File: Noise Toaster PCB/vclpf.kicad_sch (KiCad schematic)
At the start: 27 parts, among them Q5 2N5457, U2 LM324, X12 Conn_01x01_Pin

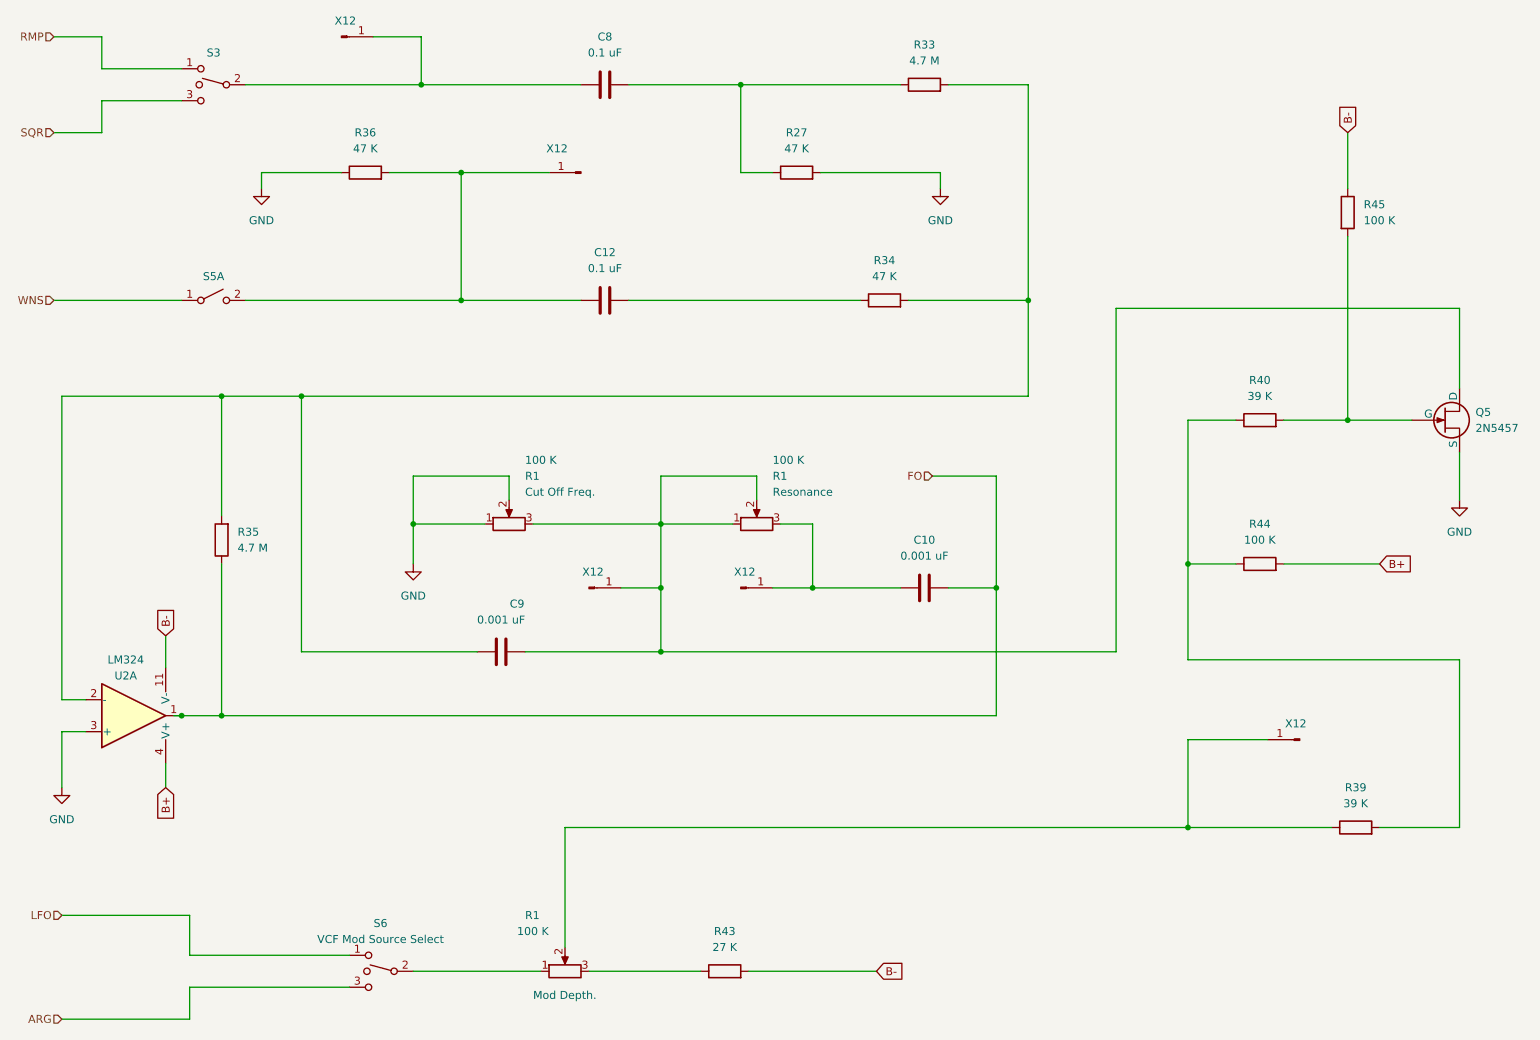
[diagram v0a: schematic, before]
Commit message: updated schematics
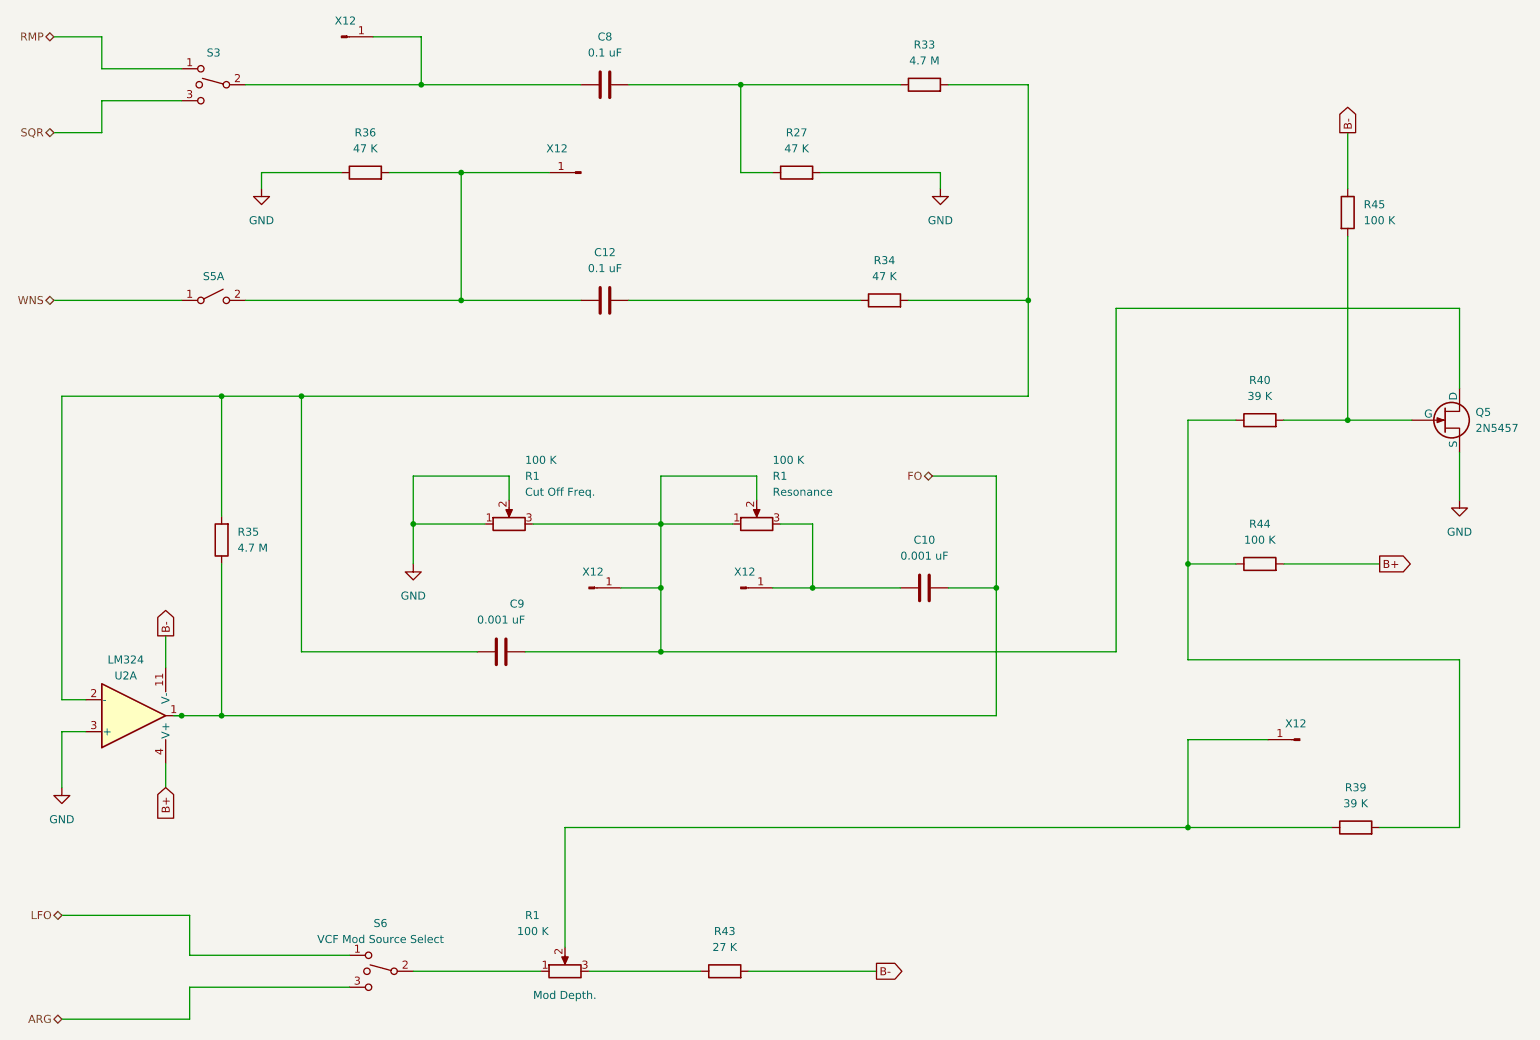
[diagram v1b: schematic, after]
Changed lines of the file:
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@@
     (stroke (width 0) (type default))
   )
-  (global_label "B-" (shape input) (at 48.26 125.73 90) (fields_autoplaced)
+  (global_label "B-" (shape output) (at 48.26 125.73 90) (fields_autoplaced)
     (effects (font (size 1.27 1.27)) (justify left))
     (property "Intersheetrefs" "${INTERSHEET_REFS}" (at 48.26 119.9024 90)
@@
     )
   )
-  (global_label "B-" (shape input) (at 236.22 45.72 90) (fields_autoplaced)
+  (global_label "B-" (shape output) (at 236.22 45.72 90) (fields_autoplaced)
     (effects (font (size 1.27 1.27)) (justify left))
     (property "Intersheetrefs" "${INTERSHEET_REFS}" (at 236.22 39.8924 90)
@@
     )
   )
-  (global_label "B+" (shape input) (at 241.3 114.3 0) (fields_autoplaced)
+  (global_label "B+" (shape output) (at 241.3 114.3 0) (fields_autoplaced)
     (effects (font (size 1.27 1.27)) (justify left))
     (property "Intersheetrefs" "${INTERSHEET_REFS}" (at 247.1276 114.3 0)
@@
     )
   )
-  (global_label "B-" (shape input) (at 161.29 179.07 0) (fields_autoplaced)
+  (global_label "B-" (shape output) (at 161.29 179.07 0) (fields_autoplaced)
     (effects (font (size 1.27 1.27)) (justify left))
     (property "Intersheetrefs" "${INTERSHEET_REFS}" (at 167.1176 179.07 0)
@@
     )
   )
-  (hierarchical_label "FO" (shape input) (at 170.18 100.33 180) (fields_autoplaced)
+  (hierarchical_label "FO" (shape bidirectional) (at 170.18 100.33 180) (fields_autoplaced)
     (effects (font (size 1.27 1.27)) (justify right))
   )
-  (hierarchical_label "SQR" (shape input) (at 30.48 45.72 180) (fields_autoplaced)
+  (hierarchical_label "SQR" (shape bidirectional) (at 30.48 45.72 180) (fields_autoplaced)
     (effects (font (size 1.27 1.27)) (justify right))
   )
-  (hierarchical_label "ARG" (shape input) (at 31.75 186.69 180) (fields_autoplaced)
+  (hierarchical_label "ARG" (shape bidirectional) (at 31.75 186.69 180) (fields_autoplaced)
     (effects (font (size 1.27 1.27)) (justify right))
   )
-  (hierarchical_label "WNS" (shape input) (at 30.48 72.39 180) (fields_autoplaced)
+  (hierarchical_label "WNS" (shape bidirectional) (at 30.48 72.39 180) (fields_autoplaced)
     (effects (font (size 1.27 1.27)) (justify right))
   )
-  (hierarchical_label "RMP" (shape input) (at 30.48 30.48 180) (fields_autoplaced)
+  (hierarchical_label "RMP" (shape bidirectional) (at 30.48 30.48 180) (fields_autoplaced)
     (effects (font (size 1.27 1.27)) (justify right))
   )
-  (hierarchical_label "LFO" (shape input) (at 31.75 170.18 180) (fields_autoplaced)
+  (hierarchical_label "LFO" (shape bidirectional) (at 31.75 170.18 180) (fields_autoplaced)
     (effects (font (size 1.27 1.27)) (justify right))
   )
@@
     (instances
       (project "Noise Toaster PCB"
-        (path "/7be3f398-d902-4566-9ee4-0bff072cd47e/9c6b1f0b-dddb-43c5-83ba-4fcd1cf28662"
-          (reference "#PWR01") (unit 1)
-        )
         (path "/7be3f398-d902-4566-9ee4-0bff072cd47e/a3e9deee-1b9d-4545-a3c9-71b211642b5b"
           (reference "#PWR04") (unit 1)
@@
     (instances
       (project "Noise Toaster PCB"
-        (path "/7be3f398-d902-4566-9ee4-0bff072cd47e/9c6b1f0b-dddb-43c5-83ba-4fcd1cf28662"
-          (reference "#PWR01") (unit 1)
-        )
         (path "/7be3f398-d902-4566-9ee4-0bff072cd47e/a3e9deee-1b9d-4545-a3c9-71b211642b5b"
           (reference "#PWR04") (unit 1)
@@
     (instances
       (project "Noise Toaster PCB"
-        (path "/7be3f398-d902-4566-9ee4-0bff072cd47e/9c6b1f0b-dddb-43c5-83ba-4fcd1cf28662"
-          (reference "#PWR01") (unit 1)
-        )
         (path "/7be3f398-d902-4566-9ee4-0bff072cd47e/a3e9deee-1b9d-4545-a3c9-71b211642b5b"
           (reference "#PWR04") (unit 1)
@@
     (instances
       (project "Noise Toaster PCB"
-        (path "/7be3f398-d902-4566-9ee4-0bff072cd47e/9c6b1f0b-dddb-43c5-83ba-4fcd1cf28662"
-          (reference "#PWR01") (unit 1)
-        )
         (path "/7be3f398-d902-4566-9ee4-0bff072cd47e/a3e9deee-1b9d-4545-a3c9-71b211642b5b"
           (reference "#PWR04") (unit 1)
@@
     (instances
       (project "Noise Toaster PCB"
-        (path "/7be3f398-d902-4566-9ee4-0bff072cd47e/9c6b1f0b-dddb-43c5-83ba-4fcd1cf28662"
-          (reference "#PWR01") (unit 1)
-        )
         (path "/7be3f398-d902-4566-9ee4-0bff072cd47e/a3e9deee-1b9d-4545-a3c9-71b211642b5b"
           (reference "#PWR04") (unit 1)

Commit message: refactored the schematic
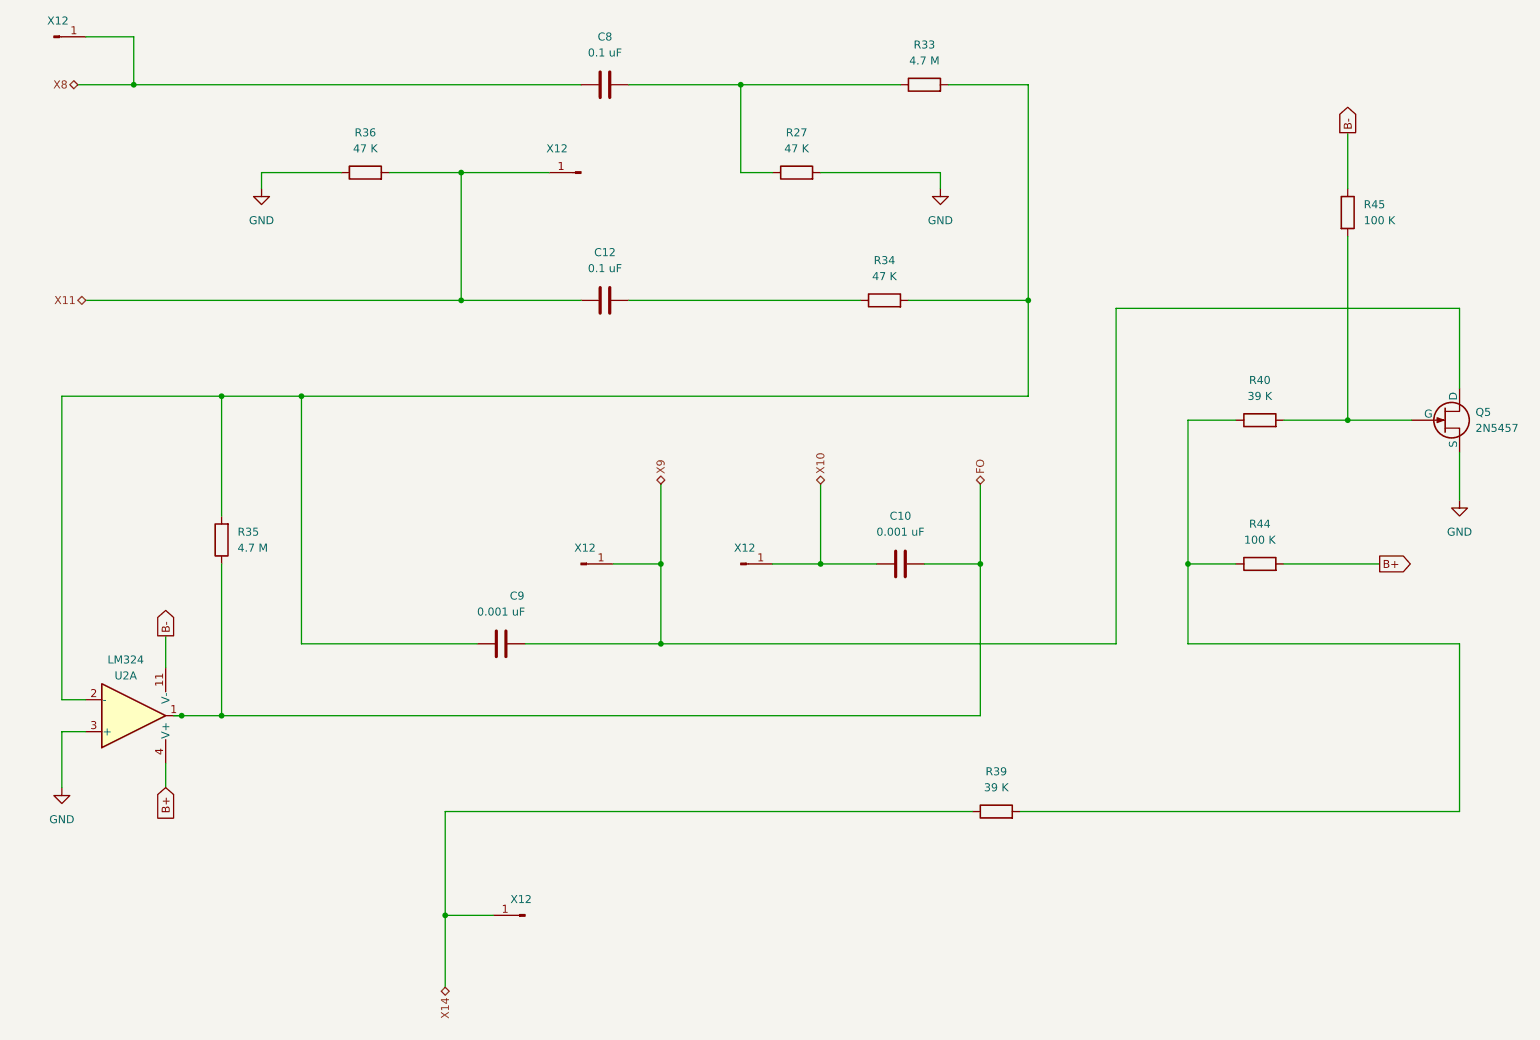
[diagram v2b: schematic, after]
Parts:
- removed R1 (x3): 100 K, symbol Device:R_Potentiometer
- removed R43: 27 K, symbol Device:R
- removed S3: ~, symbol Switch:SW_SPDT_MSM
- removed S5: ~, symbol Switch:SW_DPST_x2
- removed S6: VCF Mod Source Select, symbol Switch:SW_SPDT_MSM
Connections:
- net X14: now reaches R39.1, X12.1 (Pin_1)
- net X11: now reaches C12.1, R36.2, X12.1 (Pin_1)
- net X9: now reaches C9.1, Q5.1 (D), X12.1 (Pin_1)
- net X8: now reaches C8.1, X12.1 (Pin_1)
- net X10: now reaches C10.1, X12.1 (Pin_1)
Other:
- moved on the sheet: C10, C9, R39, X12
